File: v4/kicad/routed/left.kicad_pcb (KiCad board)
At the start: 2 copper layers, 158 x 118.6 mm, 68 parts

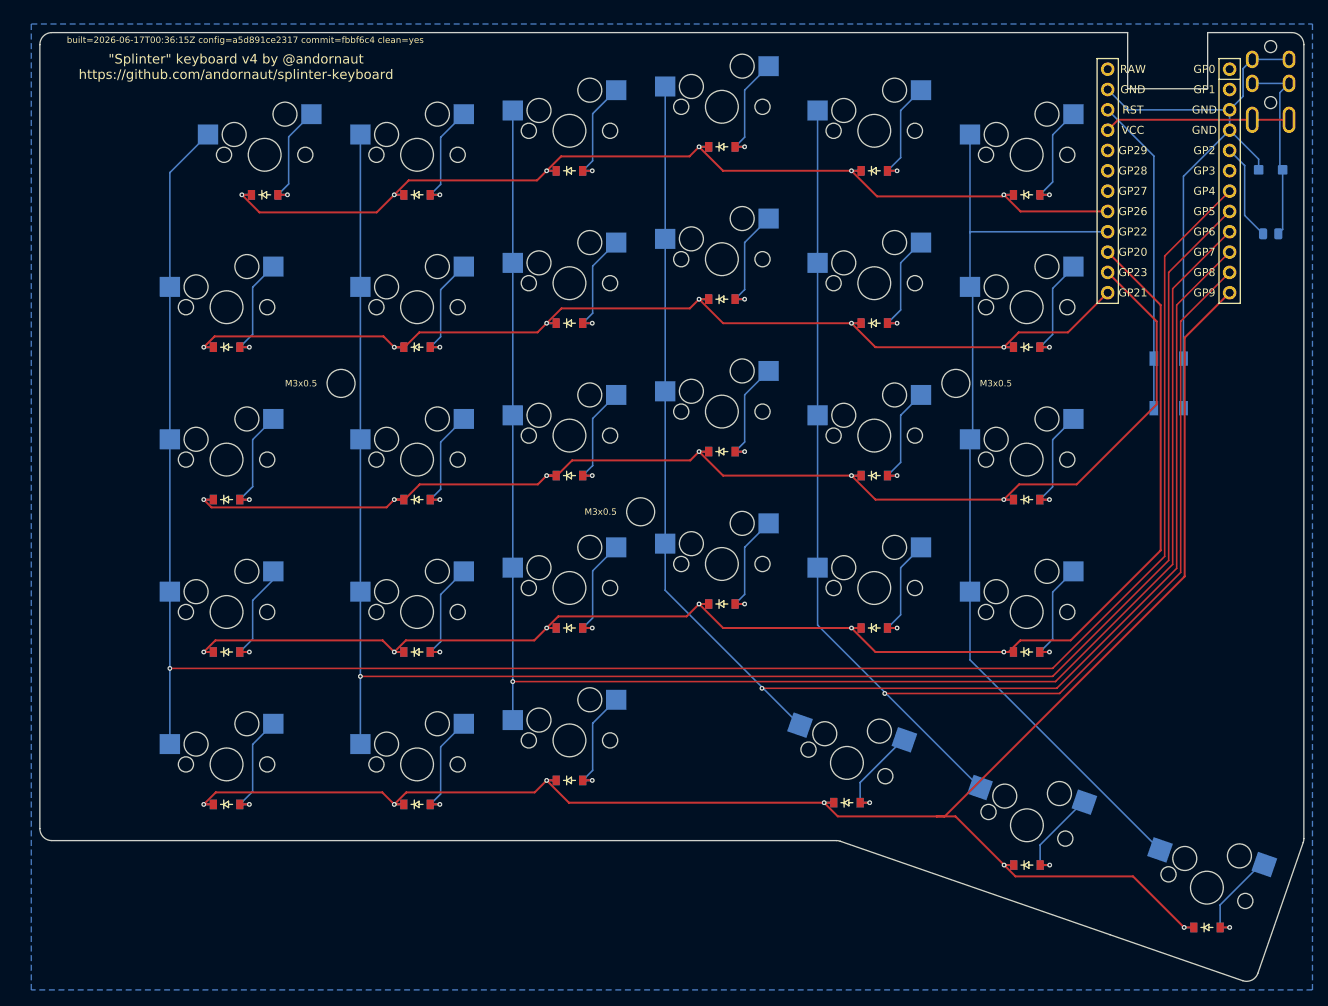
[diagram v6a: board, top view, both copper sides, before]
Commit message: v4: rebuild all boards against current config (footprint cleanups)
Full pipeline rebuild brings unrouted/ + routed/ to config=9096bb80de4e,
reflecting the recent footprint cleanups (lib prefix, side-derived via
layers, dead param). Orphaned include_traces_vias dead stubs removed
(left 385->309 segments / 65->35 vias; right 406->334 / 70->38).
Routing complete: both routed halves pass connectivity DRC (0 violations,
0 unconnected). Teardrops preserved (left 470, right ~500).
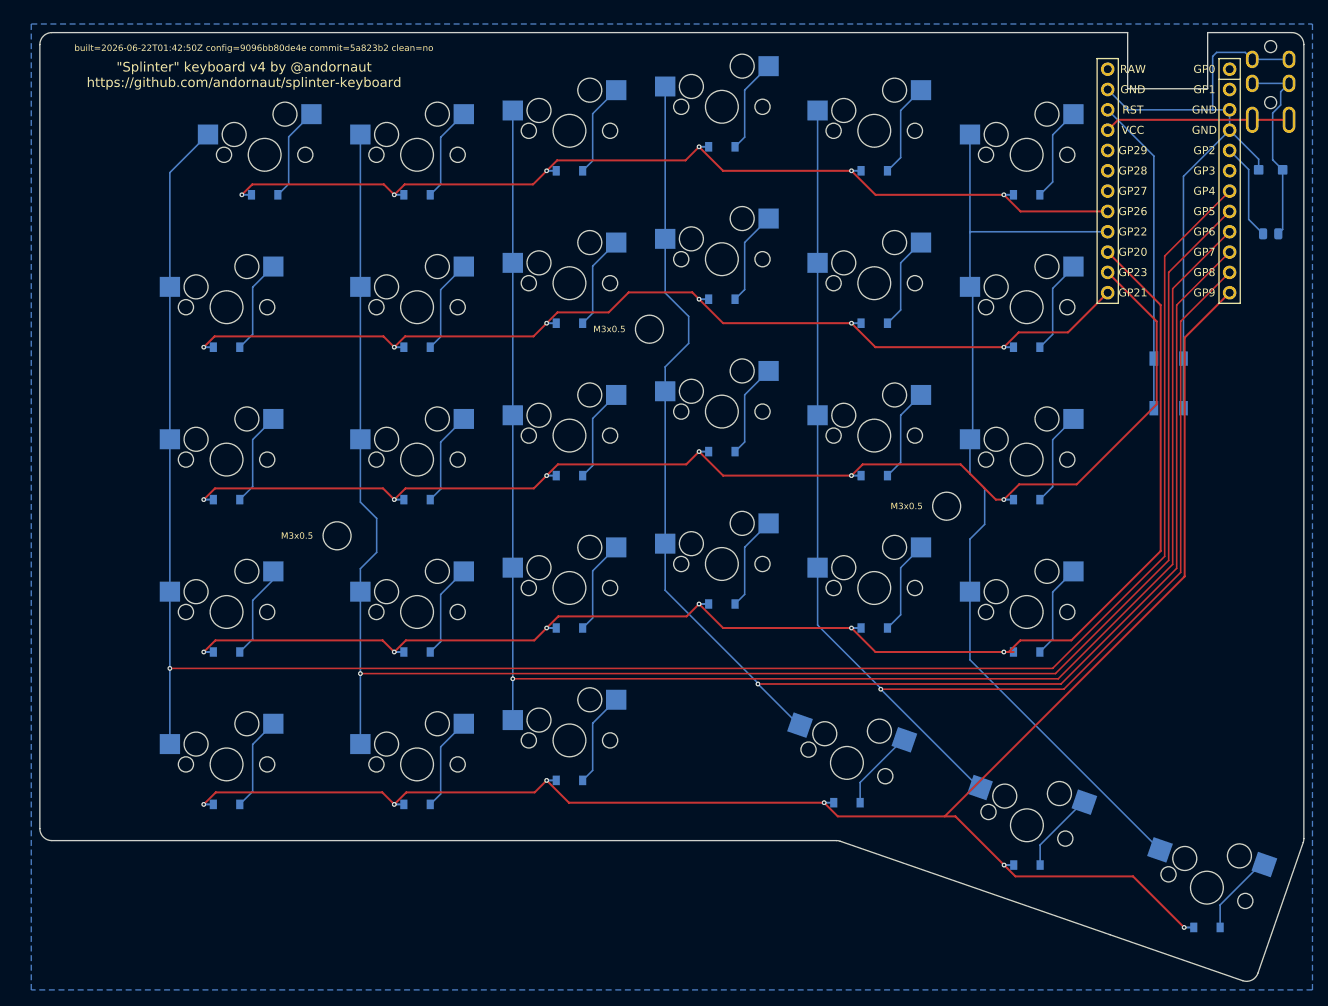
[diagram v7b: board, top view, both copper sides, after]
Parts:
- MCU1: footprint ceoloide:mcu_liatris -> splinter:mcu_liatris
- moved MH3 38.9 mm to (207.1, 126.6)
- moved MH2 38.3 mm to (244.2, 148.7)
- moved MH1 19.1 mm to (168.1, 152.4)
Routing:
- net P9: track 228.3 -> 220.1 mm
- net P18: track 130.5 -> 122.3 mm
- net P10: track 136.3 -> 129.8 mm
- net P14: track 186.1 -> 180.1 mm
- net P16: track 163.3 -> 157.6 mm
- net GND: track 74.5 -> 79.2 mm
- net P7: track 187.2 -> 189.8 mm
- net one_upper: track 14.2 -> 11.8 mm, vias 1 -> 0
- net zero_mod: track 14.2 -> 11.8 mm, vias 1 -> 0
- net zero_lower: track 13.2 -> 10.8 mm, vias 1 -> 0
- net zero_home: track 14.2 -> 11.8 mm, vias 1 -> 0
- net three_mod: track 12.5 -> 10.1 mm, vias 1 -> 0
- net one_num: track 14.2 -> 11.8 mm, vias 1 -> 0
- net one_mod: track 14.2 -> 11.8 mm, vias 1 -> 0
- net one_lower: track 14.2 -> 11.8 mm, vias 1 -> 0
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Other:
- board text added: "DATA"
- board text added: "VCC"
- board text added: "built=2026-06-22T01:42:50Z config=9096bb80de4e commit=5a823b2 clean=no"
- board text removed: "built=2026-06-17T00:36:15Z config=a5d891ce2317 commit=fbbf6c4 clean=yes"

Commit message: v4: re-stamp boards clean=yes from committed source (06c8ffa)
Full pipeline rebuild on the now-committed tree: routed + unrouted boards
carry clean=yes commit=06c8ffa, so the provenance stamp is authoritative.
config unchanged (9096bb80de4e). All gates pass: connectivity DRC clean,
GND flood present (master + gerber), full gerber set, BOM/CPL complete,
teardrops 277 left / 295 right. validate:fab passes with zero warnings.
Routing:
- net P9: track 220.1 -> 227.3 mm
- net P16: track 157.6 -> 164.8 mm
- net P10: track 129.8 -> 137.0 mm
- net P18: track 122.3 -> 129.5 mm
- net P14: track 180.1 -> 186.1 mm
- net one_upper: track 11.8 -> 14.2 mm, vias 0 -> 1
- net zero_mod: track 11.8 -> 14.2 mm, vias 0 -> 1
- net zero_lower: track 10.8 -> 13.2 mm, vias 0 -> 1
- net zero_home: track 11.8 -> 14.2 mm, vias 0 -> 1
- net three_mod: track 10.1 -> 12.5 mm, vias 0 -> 1
- net one_num: track 11.8 -> 14.2 mm, vias 0 -> 1
- net one_mod: track 11.8 -> 14.2 mm, vias 0 -> 1
- net one_lower: track 11.8 -> 14.2 mm, vias 0 -> 1
- net one_home: track 11.8 -> 14.2 mm, vias 0 -> 1
- net four_upper: track 11.8 -> 14.2 mm, vias 0 -> 1
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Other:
- board text added: "built=2026-06-22T02:28:18Z config=9096bb80de4e commit=06c8ffa clean=yes"
- board text removed: "built=2026-06-22T01:42:50Z config=9096bb80de4e commit=5a823b2 clean=no"
